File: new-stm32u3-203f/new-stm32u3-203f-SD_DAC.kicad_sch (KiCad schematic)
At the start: 11 parts, among them J1 DM3CS-SF, J2 SJ-3524-SMT, U2 TLV320DAC3203IRGER

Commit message: moved over to new sd card stuff
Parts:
- removed J1: DM3CS-SF, DM3CS-SF_HIR, symbol 2026-01-24_09-53-21:DM3CS-SF
- added J5: 473092651, CONN12_47309-2651_MOL, symbol 2026-01-28_06-17-02:473092651
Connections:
- net +3V3: now also J5.4 (VDD)
- net GNDREF: now also J5.6 (VSS), J5.G1, J5.G2, J5.G3, J5.G4
- net SD_CLK: now also J5.5 (CLK)
- net SD_CMD: now also J5.3 (CMD)
- net SD_DAT0: now also J5.7 (DAT0)
- net SD_DAT1: now also J5.8 (DAT1)
- net SD_DAT2: now also J5.1 (DAT2)
- net SD_DAT3: now also J5.2 (CD/DAT3)
- no-connect marks 4 -> 3

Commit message: finished the schematic, just need someone to review it :)
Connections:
- no-connect marks 3 -> 9
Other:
- moved on the sheet: C12, C13
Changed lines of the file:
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@@
+	)
+	(no_connect
+		(at 198.12 68.58)
+	)
+	(no_connect
+		(at 198.12 76.2)
+	)
+	(no_connect
+		(at 198.12 53.34)
+	)
+	(no_connect
+		(at 161.29 34.29)
+	)
+	(no_connect
+		(at 198.12 78.74)
 	)
 	(no_connect
@@
 	)
 	(no_connect
+		(at 198.12 71.12)
+	)
+	(no_connect
 		(at 121.92 66.04)
 	)
@@
 	(wire
 		(pts
-			(xy 170.18 39.37) (xy 172.72 39.37)
+			(xy 173.99 39.37) (xy 176.53 39.37)
 		)
 		(stroke
@@
 	(wire
 		(pts
-			(xy 170.18 31.75) (xy 172.72 31.75)
+			(xy 173.99 31.75) (xy 176.53 31.75)
 		)
 		(stroke
@@
 	(wire
 		(pts
-			(xy 161.29 39.37) (xy 162.56 39.37)
+			(xy 161.29 39.37) (xy 166.37 39.37)
 		)
 		(stroke
@@
 	(wire
 		(pts
-			(xy 161.29 31.75) (xy 162.56 31.75)
+			(xy 161.29 31.75) (xy 166.37 31.75)
 		)
 		(stroke
@@
 	(global_label "HP_RIGHT"
 		(shape input)
-		(at 172.72 31.75 0)
+		(at 176.53 31.75 0)
 		(fields_autoplaced yes)
 		(effects
@@
 		)
 		(property "Intersheetrefs" "${INTERSHEET_REFS}"
-			(at 184.7162 31.75 0)
+			(at 188.5262 31.75 0)
 			(effects
 				(font
@@
 	(global_label "HP_LEFT"
 		(shape input)
-		(at 172.72 39.37 0)
+		(at 176.53 39.37 0)
 		(fields_autoplaced yes)
 		(effects
@@
 		)
 		(property "Intersheetrefs" "${INTERSHEET_REFS}"
-			(at 183.5066 39.37 0)
+			(at 187.3166 39.37 0)
 			(effects
 				(font
@@
 	(symbol
 		(lib_id "Device:C")
-		(at 166.37 39.37 90)
+		(at 170.18 39.37 90)
 		(unit 1)
 		(exclude_from_sim no)
@@
 		(dnp no)
 		(property "Reference" "C13"
-			(at 163.322 38.354 90)
+			(at 167.132 38.354 90)
 			(effects
 				(font
@@
 		)
 		(property "Value" "47u"
-			(at 169.164 38.354 90)
+			(at 172.974 38.354 90)
 			(effects
 				(font
@@
 		)
 		(property "Footprint" ""
-			(at 170.18 38.4048 0)
+			(at 173.99 38.4048 0)
 			(effects
 				(font
@@
 		)
 		(property "Datasheet" "~"
-			(at 166.37 39.37 0)
+			(at 170.18 39.37 0)
 			(effects
 				(font
@@
 		)
 		(property "Description" "Unpolarized capacitor"
-			(at 166.37 39.37 0)
+			(at 170.18 39.37 0)
 			(effects
 				(font
@@
 	(symbol
 		(lib_id "Device:C")
-		(at 166.37 31.75 90)
+		(at 170.18 31.75 90)
 		(unit 1)
 		(exclude_from_sim no)
@@
 		(dnp no)
 		(property "Reference" "C12"
-			(at 163.322 30.734 90)
+			(at 167.132 30.734 90)
 			(effects
 				(font
@@
 		)
 		(property "Value" "47u"
-			(at 169.418 30.734 90)
+			(at 173.228 30.734 90)
 			(effects
 				(font
@@
 		)
 		(property "Footprint" ""
-			(at 170.18 30.7848 0)
+			(at 173.99 30.7848 0)
 			(effects
 				(font
@@
 		)
 		(property "Datasheet" "~"
-			(at 166.37 31.75 0)
+			(at 170.18 31.75 0)
 			(effects
 				(font
@@
 		)
 		(property "Description" "Unpolarized capacitor"
-			(at 166.37 31.75 0)
-			(effects
-				(font
+			(at 170.18 31.75 0)
+			(effects
+				(font

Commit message: added reset button. asigned footprints.
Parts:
- C12, C13, C14, C15, C16, C17, C18, C8: footprint (none) -> Capacitor_SMD:C_0603_1608Metric
- J5: footprint CONN12_47309-2651_MOL -> footprints_sd:CONN12_47309-2651_MOL
- U2: footprint RGE24_2P7X2P7_TEX -> Package_DFN_QFN:Texas_RGE0024C_VQFN-24-1EP_4x4mm_P0.5mm_EP2.1x2.1mm
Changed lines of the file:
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@@
 			)
 		)
-		(property "Footprint" ""
+		(property "Footprint" "Capacitor_SMD:C_0603_1608Metric"
 			(at 173.99 38.4048 0)
 			(effects
@@
 			)
 		)
-		(property "Footprint" ""
+		(property "Footprint" "Capacitor_SMD:C_0603_1608Metric"
 			(at 225.0948 87.63 0)
 			(effects
@@
 			)
 		)
-		(property "Footprint" ""
+		(property "Footprint" "Capacitor_SMD:C_0603_1608Metric"
 			(at 226.3648 57.15 0)
 			(effects
@@
 			)
 		)
-		(property "Footprint" ""
+		(property "Footprint" "Capacitor_SMD:C_0603_1608Metric"
 			(at 216.2048 57.15 0)
 			(effects
@@
 			)
 		)
-		(property "Footprint" "RGE24_2P7X2P7_TEX"
+		(property "Footprint" "Package_DFN_QFN:Texas_RGE0024C_VQFN-24-1EP_4x4mm_P0.5mm_EP2.1x2.1mm"
 			(at 121.92 53.34 0)
 			(effects
@@
 			)
 		)
-		(property "Footprint" "CONN12_47309-2651_MOL"
+		(property "Footprint" "footprints_sd:CONN12_47309-2651_MOL"
 			(at 54.61 60.96 0)
 			(effects
@@
 			)
 		)
-		(property "Footprint" ""
+		(property "Footprint" "Capacitor_SMD:C_0603_1608Metric"
 			(at 214.9348 87.63 0)
 			(effects
@@
 			)
 		)
-		(property "Footprint" ""
+		(property "Footprint" "Capacitor_SMD:C_0603_1608Metric"
 			(at 68.2752 45.72 0)
 			(effects
@@
 			)
 		)
-		(property "Footprint" ""
+		(property "Footprint" "Capacitor_SMD:C_0603_1608Metric"
 			(at 173.99 30.7848 0)
 			(effects
@@
 			)
 		)
-		(property "Footprint" ""
+		(property "Footprint" "Capacitor_SMD:C_0603_1608Metric"
 			(at 208.28 72.6948 0)
 			(effects

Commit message: made some progress on the pcb
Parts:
- J2: footprint SJ-3524-SMT:CUI_SJ-3524-SMT -> Connector_Audio:Jack_3.5mm_CUI_SJ-3524-SMT_Horizontal
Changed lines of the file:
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@@
 			)
 		)
-		(property "Footprint" "SJ-3524-SMT:CUI_SJ-3524-SMT"
+		(property "Footprint" "Connector_Audio:Jack_3.5mm_CUI_SJ-3524-SMT_Horizontal"
 			(at 148.59 34.29 0)
 			(effects

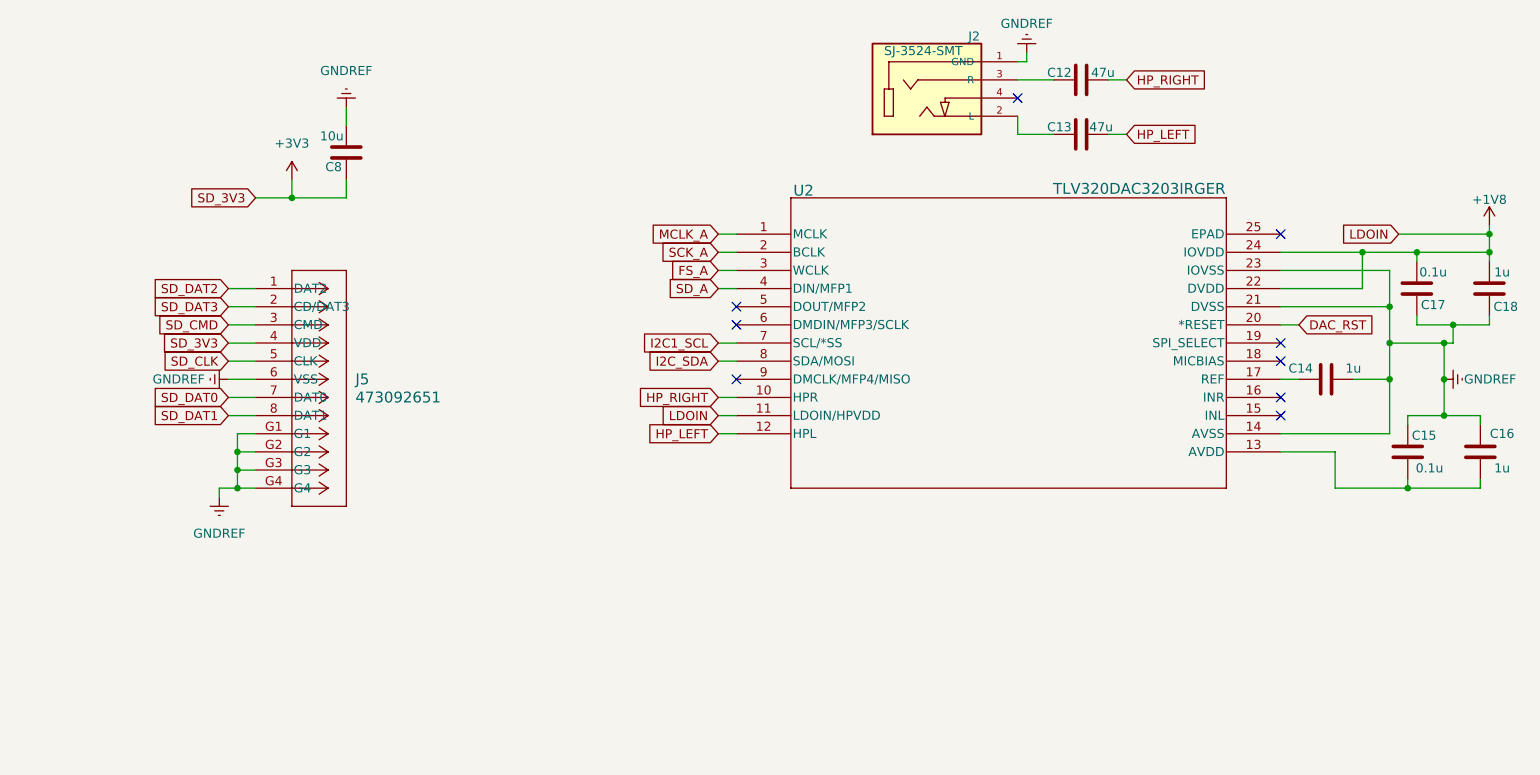
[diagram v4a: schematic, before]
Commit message: added in 0r to choose ldoin of dac
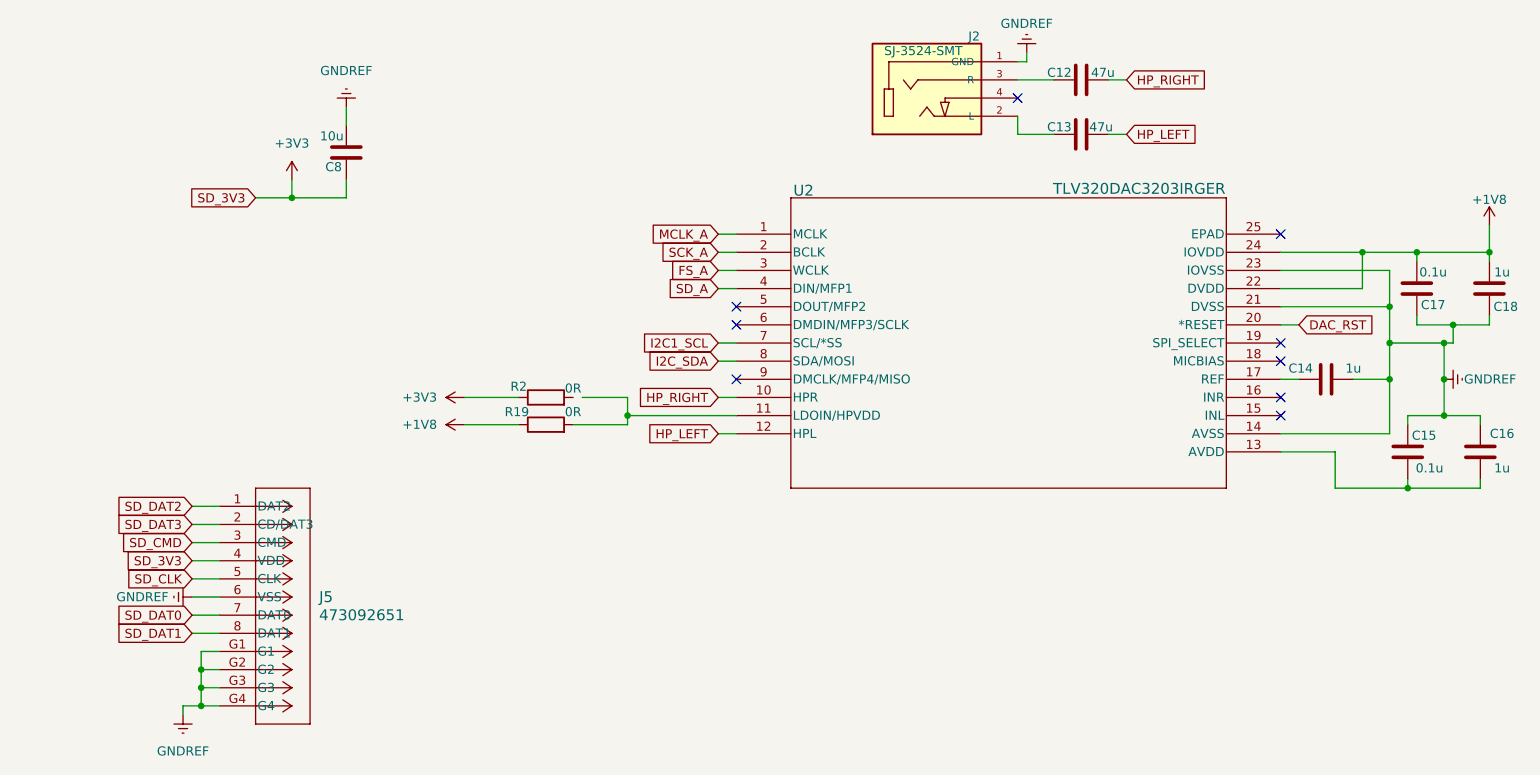
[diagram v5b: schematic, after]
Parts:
- added R19, R2: 0R, Resistor_SMD:R_0603_1608Metric, symbol Device:R
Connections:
- net +1V8: now also R19.1; no longer U2.11 (LDOIN/HPVDD)
- net +3V3: now also R2.1
- new net: R19.2, U2.11 (LDOIN/HPVDD)
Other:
- moved on the sheet: J5

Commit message: made routing progress
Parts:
- C15, C17: value 0.1u -> 1u
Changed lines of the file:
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@@
 			)
 		)
-		(property "Value" "0.1u"
+		(property "Value" "1u"
 			(at 219.456 58.674 0)
 			(effects
@@
 			)
 		)
-		(property "Value" "0.1u"
+		(property "Value" "1u"
 			(at 218.948 86.106 0)
 			(effects

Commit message: made some better progress routing
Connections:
- net at R2.2: now also R19.2, U2.11 (LDOIN/HPVDD)
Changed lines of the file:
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@@
+	(wire
+		(pts
+			(xy 99.06 76.2) (xy 106.68 76.2)
+		)
+		(stroke
+			(width 0)
+			(type default)
+		)
+	)
 	(wire
 		(pts
@@
 		)
 		(stroke
-			(width 0)
-			(type default)
-		)
-	)
-	(wire
-		(pts
-			(xy 100.33 76.2) (xy 106.68 76.2)
-		)
-		(stroke
